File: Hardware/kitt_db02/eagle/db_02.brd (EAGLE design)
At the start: 50 x 11 mm, 32 parts, among them J1 FTS-109-01-L-DV, T8.1 TPTP09SQ, T8.2 TPTP09SQ, U8.0 MCP23017ML, X8.1 CON_HEADER_1X08-SMD

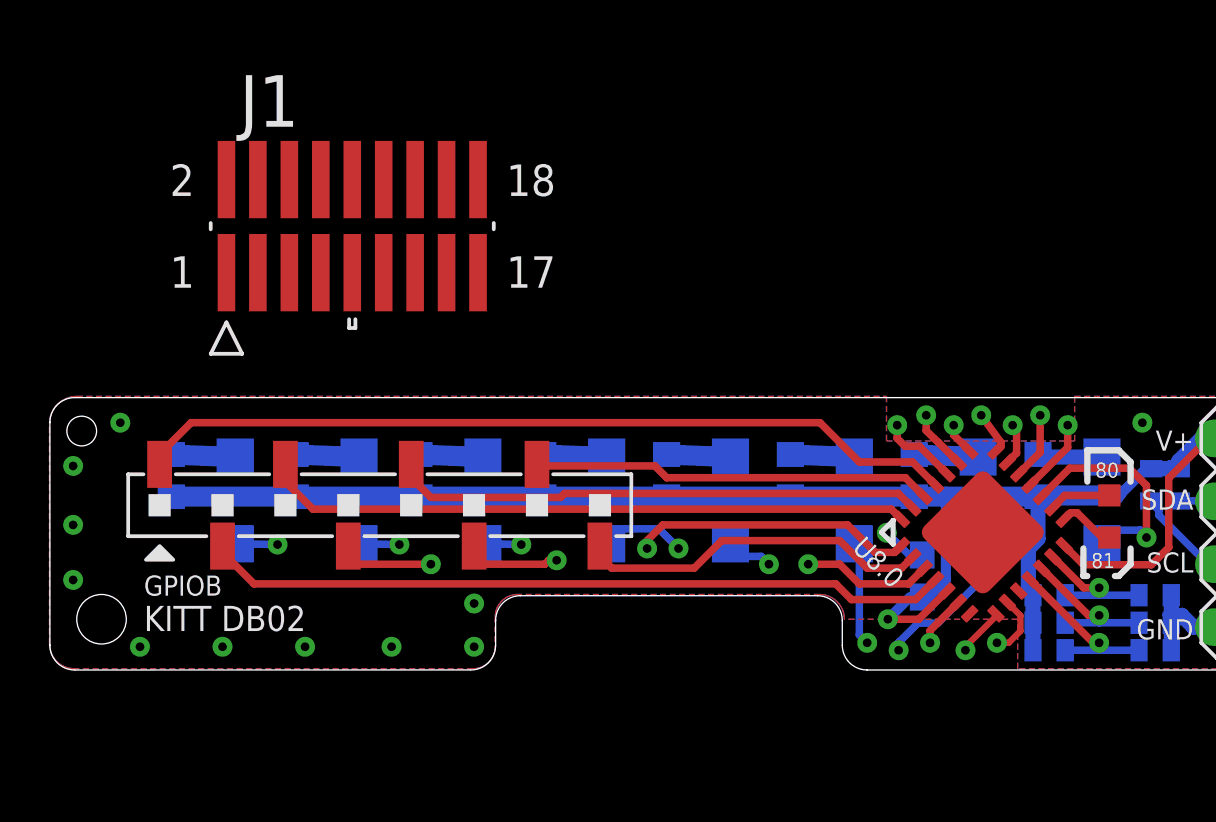
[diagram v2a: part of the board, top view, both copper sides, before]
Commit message: snapshot of db02 board layout : this is going nowhere edition -> reverting back to previous version
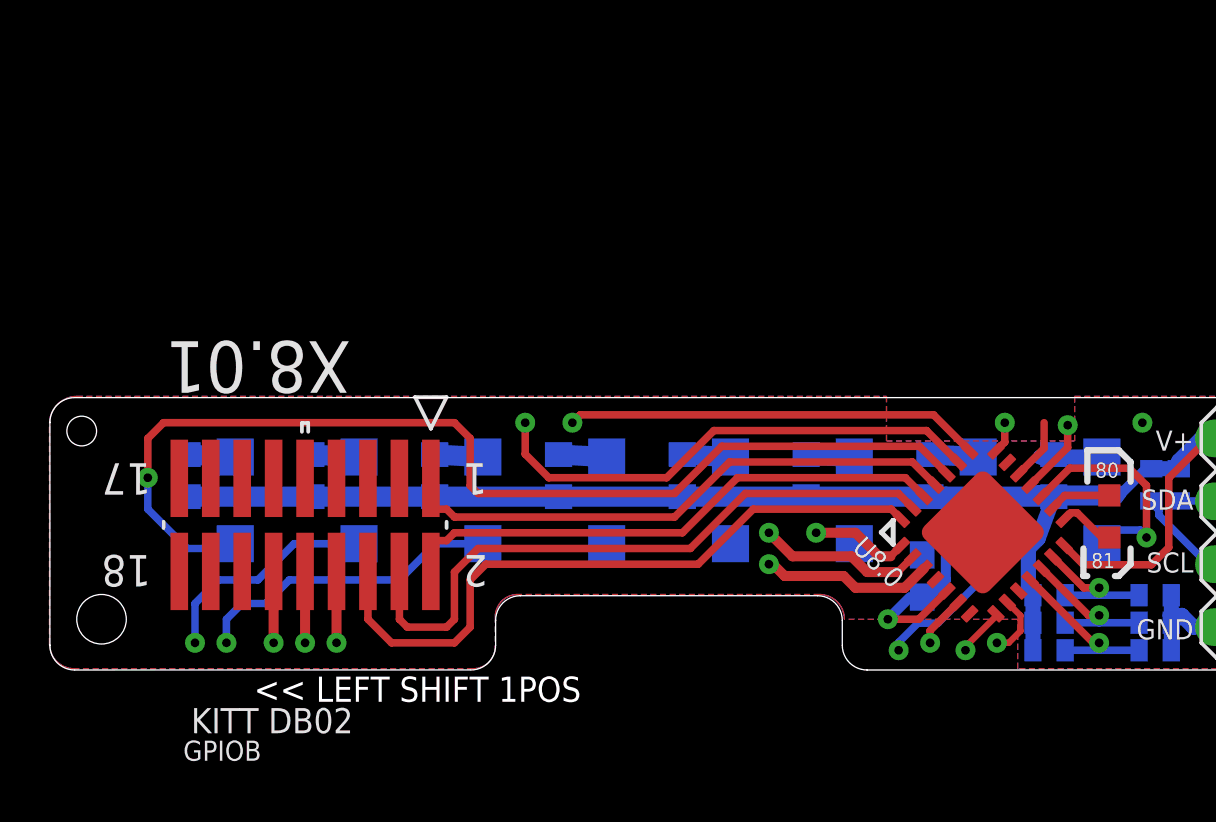
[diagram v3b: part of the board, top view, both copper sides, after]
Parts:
- removed J1: FTS-109-01-L-DV, kitt.con:SAMTEC_FTS-109-01-L-DV
- removed X8.1: CON_HEADER_1X08-SMD, dp_devices:M1X8_SMD
- added X8.01: FTS-109-01-L-DV, kitt.con:SAMTEC_FTS-109-01-L-DV
- moved R8.0 0.63 mm to (144.5, 89.6)
- moved R8.1 0.63 mm to (139.5, 89.6)
- moved R8.2 0.63 mm to (134.5, 89.6)
- moved R8.3 0.63 mm to (129.5, 89.6)
- moved R8.4 0.63 mm to (124.5, 89.6)
- moved R8.5 0.63 mm to (119.5, 89.6)
- moved R8.6 0.63 mm to (114.5, 89.6)
- moved R8.7 0.63 mm to (109.5, 89.6)
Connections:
- net GPB0: now also X8.01.1; no longer X8.1.1
- net GPB1: now also X8.01.2; no longer X8.1.7
- net GPB2: now also X8.01.4; no longer X8.1.5
- net GPB3: now also X8.01.6; no longer X8.1.3
- net GPB4: now also X8.01.12; no longer X8.1.6
- net GPB5: now also X8.01.10; no longer X8.1.8
- net GPB6: now also X8.01.8; no longer X8.1.4
- net GPB7: now also X8.01.14; no longer X8.1.2
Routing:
- net GPB7: track 30.2 -> 0.00 mm
- net N$6: track 22.1 -> 47.8 mm
- net N$7: track 27.0 -> 46.6 mm
- net N$3: track 20.6 -> 2.49 mm, vias 2 -> 0
- net N$4: track 17.5 -> 0.35 mm, vias 2 -> 0
- net GPB5: track 15.0 -> 30.7 mm, vias 0 -> 2
- net GPB4: track 19.3 -> 34.3 mm
- net N$8: track 30.6 -> 43.2 mm, vias 2 -> 1
- net GPB0: track 33.3 -> 23.1 mm
- net GPB1: track 16.1 -> 22.5 mm
- net GPB2: track 21.4 -> 26.4 mm
- net GPB6: track 25.2 -> 29.4 mm
- net N$5: track 21.2 -> 18.0 mm, vias 2 -> 1
- net GND: track 11.3 -> 9.54 mm, vias 16 -> 5
- net GPB3: track 26.2 -> 27.4 mm
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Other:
- board text added: "<< LEFT SHIFT 1POS"

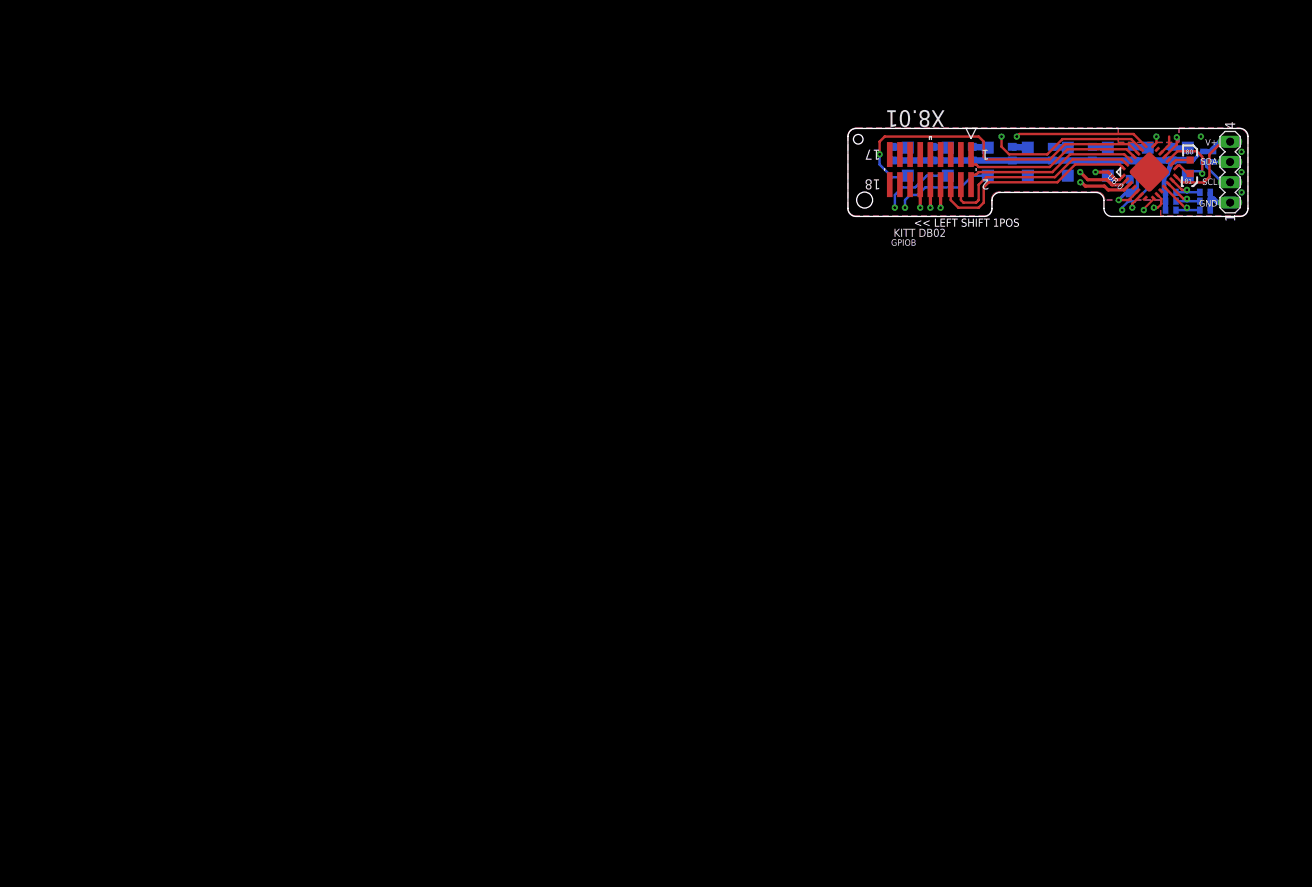
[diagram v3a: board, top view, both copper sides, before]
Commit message: restored db02 board layout from commit acb6896f0427ddee216c2485e595b1a3f3064529
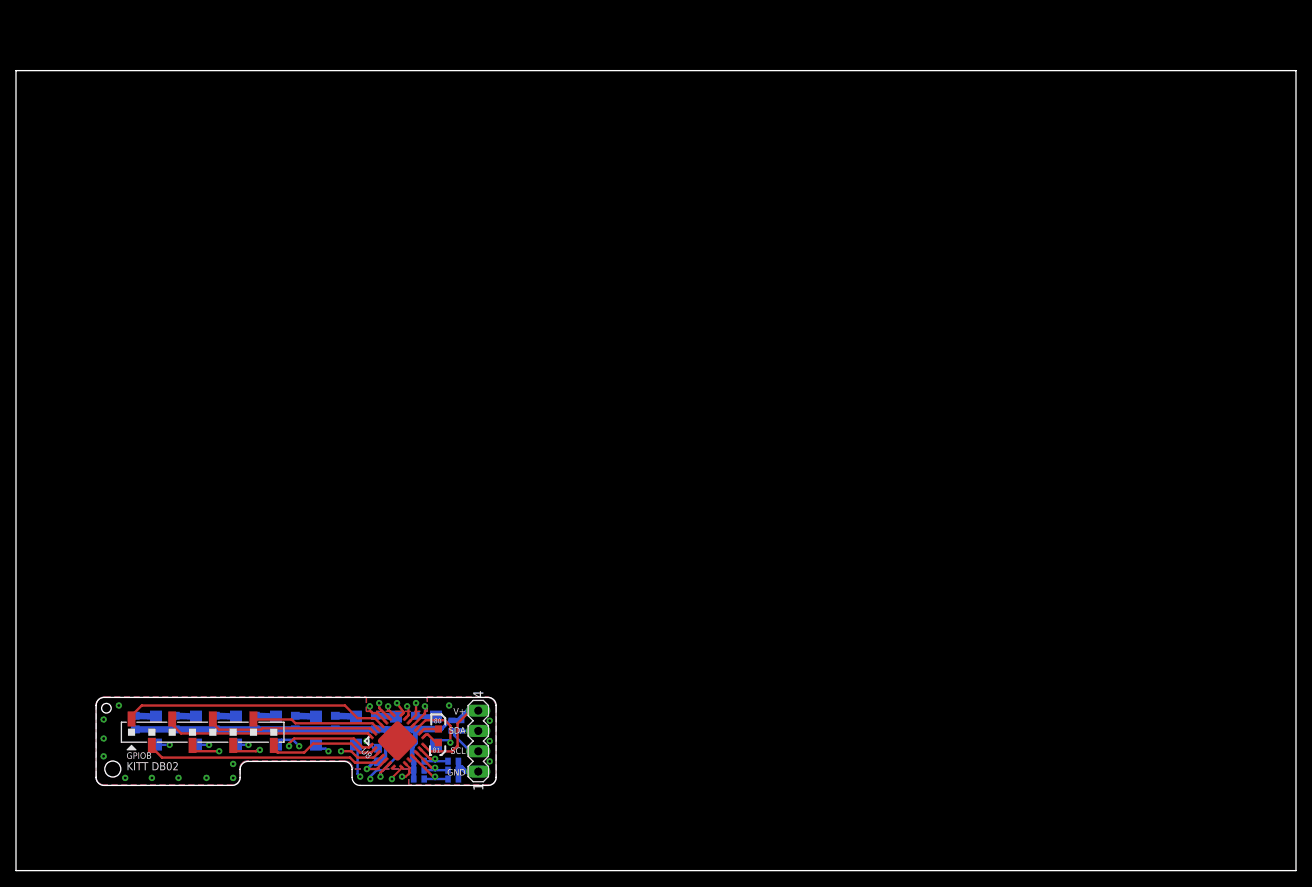
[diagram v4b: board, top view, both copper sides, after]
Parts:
- removed U$1: (no value), frames:A4L-LOC
- removed U8.0: MCP23017ML, microchip:QFN28-ML_6X6MM
- removed X8.01: FTS-109-01-L-DV, kitt.con:SAMTEC_FTS-109-01-L-DV
- added U8: MCP23017ML, microchip:QFN28-ML_6X6MM
- added X8.1: CON_HEADER_1X08-SMD, dp_devices:M1X8_SMD
- moved R8.0 118.4 mm to (49.9, 18.5)
- moved R8.1 118.4 mm to (44.9, 18.5)
- moved R8.2 118.4 mm to (39.9, 18.5)
- moved R8.3 118.4 mm to (34.9, 18.5)
- moved R8.4 118.4 mm to (29.9, 18.5)
- moved R8.5 118.4 mm to (24.9, 18.5)
- moved R8.6 118.4 mm to (19.9, 18.5)
- moved R8.7 118.4 mm to (14.9, 18.5)
- moved R8.14 117.9 mm to (55.6, 18.1)
- moved C8.0 117.9 mm to (45.2, 14.4)
- moved D8.0 117.9 mm to (52.5, 17.5)
- moved D8.1 117.9 mm to (47.5, 17.5)
- moved D8.2 117.9 mm to (42.5, 17.5)
- moved D8.3 117.9 mm to (37.5, 17.5)
- moved D8.4 117.9 mm to (32.5, 17.5)
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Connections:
- net GND: now also U8.6; no longer U8.0.6
- net GPB0: now also U8.25, X8.1.1; no longer U8.0.25, X8.01.1
- net GPB1: now also U8.26, X8.1.7; no longer U8.0.26, X8.01.2
- net GPB2: now also U8.27, X8.1.5; no longer U8.0.27, X8.01.4
- net GPB3: now also U8.28, X8.1.3; no longer U8.0.28, X8.01.6
- net GPB4: now also U8.1, X8.1.6; no longer U8.0.1, X8.01.12
- net GPB5: now also U8.2, X8.1.8; no longer U8.0.2, X8.01.10
- net GPB6: now also U8.3, X8.1.4; no longer U8.0.3, X8.01.8
- net GPB7: now also U8.4, X8.1.2; no longer U8.0.4, X8.01.14
- net N$1: now also U8.17; no longer U8.0.17
- net N$17: now also U8.11; no longer U8.0.11
- net N$18: now also U8.12; no longer U8.0.12
- net N$19: now also U8.13; no longer U8.0.13
- net N$2: now also U8.18; no longer U8.0.18
- net N$23: now also U8.16; no longer U8.0.16
- net N$24: now also U8.15; no longer U8.0.15
- net N$3: now also U8.19; no longer U8.0.19
- net N$4: now also U8.20; no longer U8.0.20
- net N$5: now also U8.21; no longer U8.0.21
- net N$6: now also U8.22; no longer U8.0.22
- net N$7: now also U8.23; no longer U8.0.23
- net N$8: now also U8.24; no longer U8.0.24
- net SCL: now also U8.9; no longer U8.0.9
- net SDA: now also U8.8; no longer U8.0.8
- net V+: now also U8.14, U8.5; no longer U8.0.14, U8.0.5
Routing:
- net GPB7: track 0.00 -> 30.2 mm
- net N$6: track 47.8 -> 22.1 mm
- net N$7: track 46.6 -> 27.0 mm
- net N$3: track 2.49 -> 20.6 mm, vias 0 -> 2
- net N$4: track 0.35 -> 17.5 mm, vias 0 -> 2
- net GPB5: track 30.7 -> 15.0 mm, vias 2 -> 0
- net GPB4: track 34.3 -> 19.3 mm
- net N$8: track 43.2 -> 30.6 mm, vias 1 -> 2
- net GPB0: track 23.1 -> 33.3 mm
- net GPB1: track 22.5 -> 16.1 mm
- net GPB2: track 26.4 -> 21.4 mm
- net GPB6: track 29.4 -> 25.2 mm
- net N$5: track 18.0 -> 21.2 mm, vias 1 -> 2
- net GND: track 9.54 -> 11.3 mm, vias 5 -> 16
- net GPB3: track 27.4 -> 26.2 mm
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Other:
- board size 50 x 11 mm -> 160 x 100 mm
- board text removed: "<< LEFT SHIFT 1POS"
